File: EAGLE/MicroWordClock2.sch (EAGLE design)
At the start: 83 parts, among them J1 DS3231S#T&RMODULE, J2 10118193-0001LF, J3 AVR_SPI_PROG_3X2PTH, U1 ATMEGA328P

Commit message: fixing the erc and drc of AVCC
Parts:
- U$1, U$10, U$11, U$12, U$13, U$14, U$15, U$16, U$17, U$18, U$19, U$2, U$20, U$21, U$22, U$23, U$24, U$25, U$26, U$27, U$28, U$29, U$3, U$30, U$31, U$32, U$33, U$34, U$35, U$36, U$37, U$38, U$39, U$4, U$40, U$41, U$42, U$43, U$44, U$45, U$46, U$47, U$48, U$49, U$5, U$50, U$51, U$52, U$53, U$54, U$55, U$56, U$57, U$58, U$59, U$6, U$60, U$61, U$62, U$63, U$64, U$7, U$8, U$9: value (none) -> WHITE
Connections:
- net +5V: now also U1.AVCC

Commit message: initial routing + pours. created a variant for the no pops
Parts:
- added J4, J5, J6, J7: (no value), SparkFun-Connectors:CONN_08"

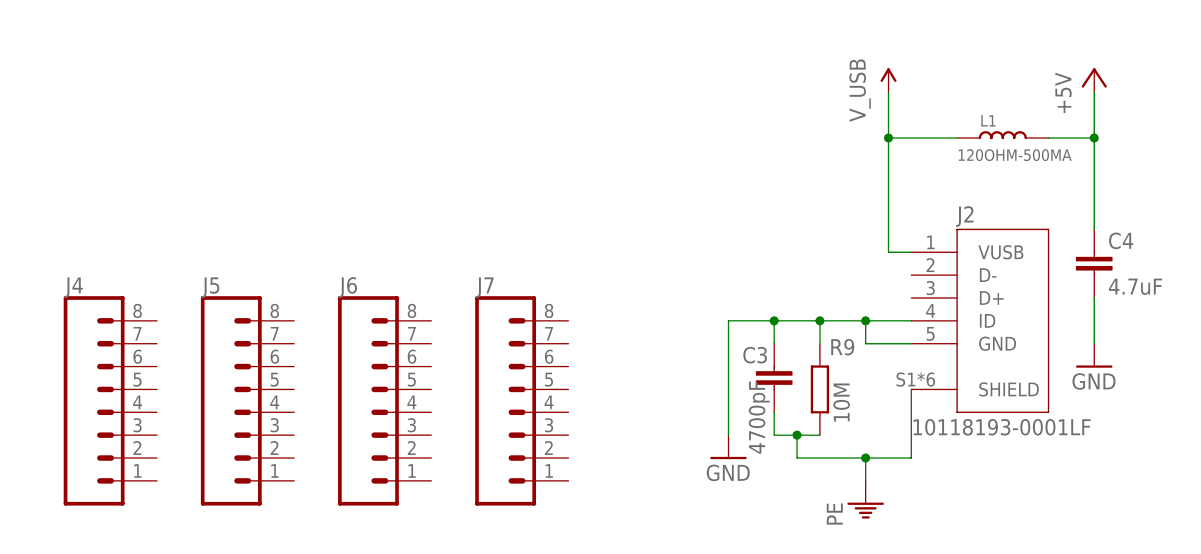
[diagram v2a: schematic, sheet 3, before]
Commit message: Fixing initial bugs from V0 - pad sizes, SCL/SDA line switch see issue #4 for full list. Also added updated schematic"
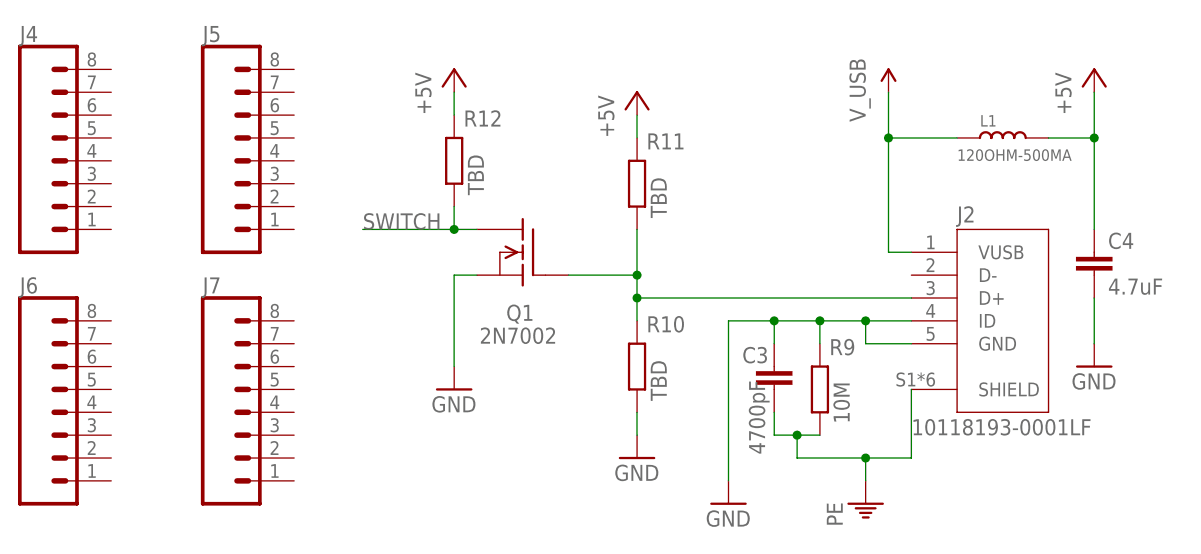
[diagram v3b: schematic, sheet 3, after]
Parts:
- added Q1: 2N7002, 2N7002:2N7002
- added R10, R11, R12: TBD, rcl:R-EU_R0603
- C1: device rcl:C-EUC0805 -> rcl:C-EUC0603
- C2: device rcl:CPOL-EUB/3528-21R -> rcl:C-EUC0603
- R1, R2, R3, R4, R5, R6, R7, R8: value 470 -> 51
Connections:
- new net SWITCH: Q1.D, R12.1, S1.1, U1.PD7(AIN1)
- net +5V: now also C2.1, R11.2, R12.2; no longer C2.+
- net GND: now also C2.2, Q1.S, R10.1; no longer C2.-
- net N$1: now also J2.D+, Q1.G, R10.2, R11.1; no longer S1.1, U1.PD7(AIN1)
- net SCL: now also J1.SCL; no longer J1.SDA
- net SDA: now also J1.SDA; no longer J1.SCL
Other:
- moved on the sheet: C1, J1, J4, J5, J6, J7
